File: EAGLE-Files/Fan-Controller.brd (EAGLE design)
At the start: 13.9 x 18.7 mm, 5 parts, among them T1 BC337

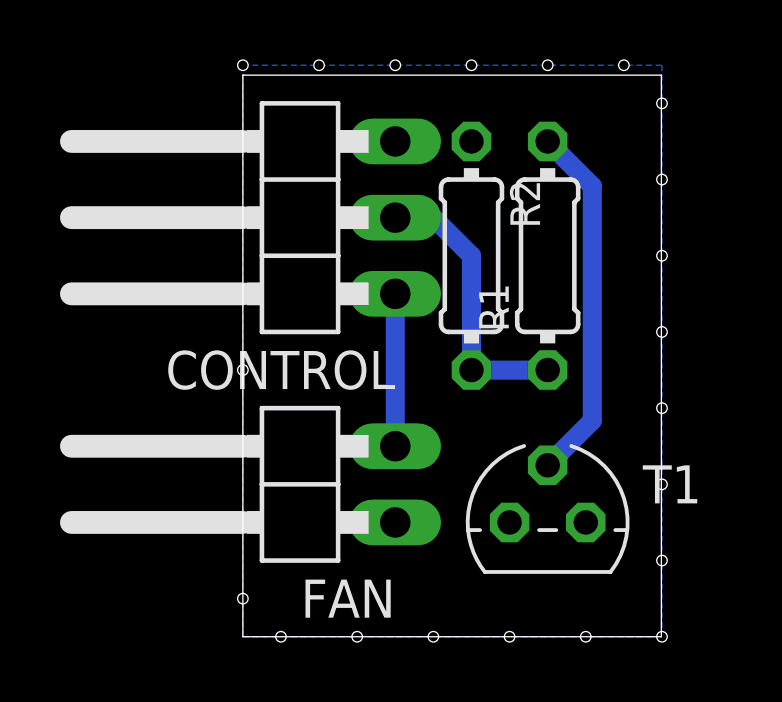
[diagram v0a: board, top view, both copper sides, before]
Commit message: Updated all boards for JLCPCB order
Also added the controller boards and schematics back
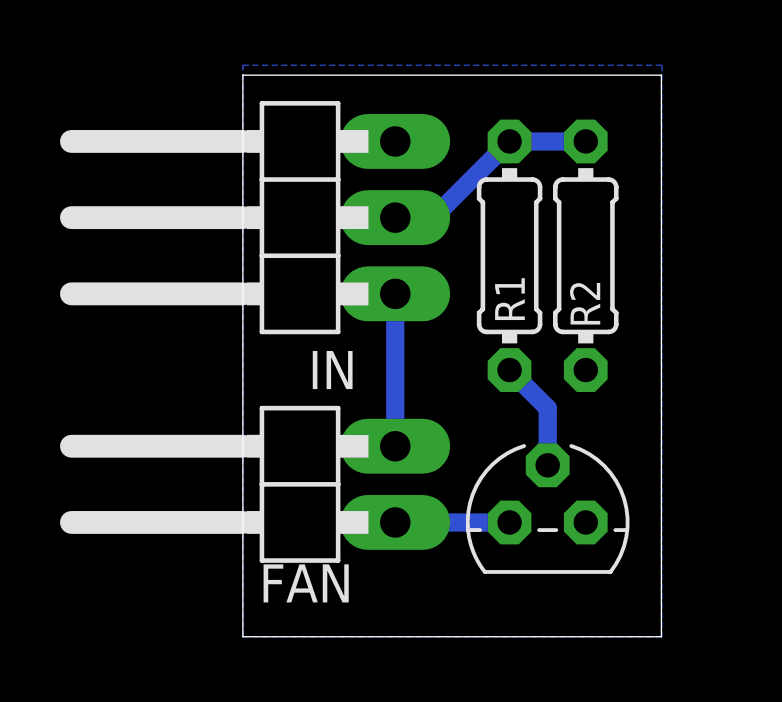
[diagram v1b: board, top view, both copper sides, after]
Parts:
- moved R2 3.81 mm to (11.4, 12.7), turned to 90 degrees
- moved R1 1.27 mm to (8.89, 12.7), turned to 270 degrees
- renumbered CONTROL to IN
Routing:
- net N$2: track 12.0 -> 3.70 mm
- net N$1: track 0.00 -> 3.81 mm
- net N$3: track 9.42 -> 7.40 mm
